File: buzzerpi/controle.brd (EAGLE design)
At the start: 100 x 80 mm, 10 parts, among them IC1 ULN2003AN, IC2 ULN2003AN

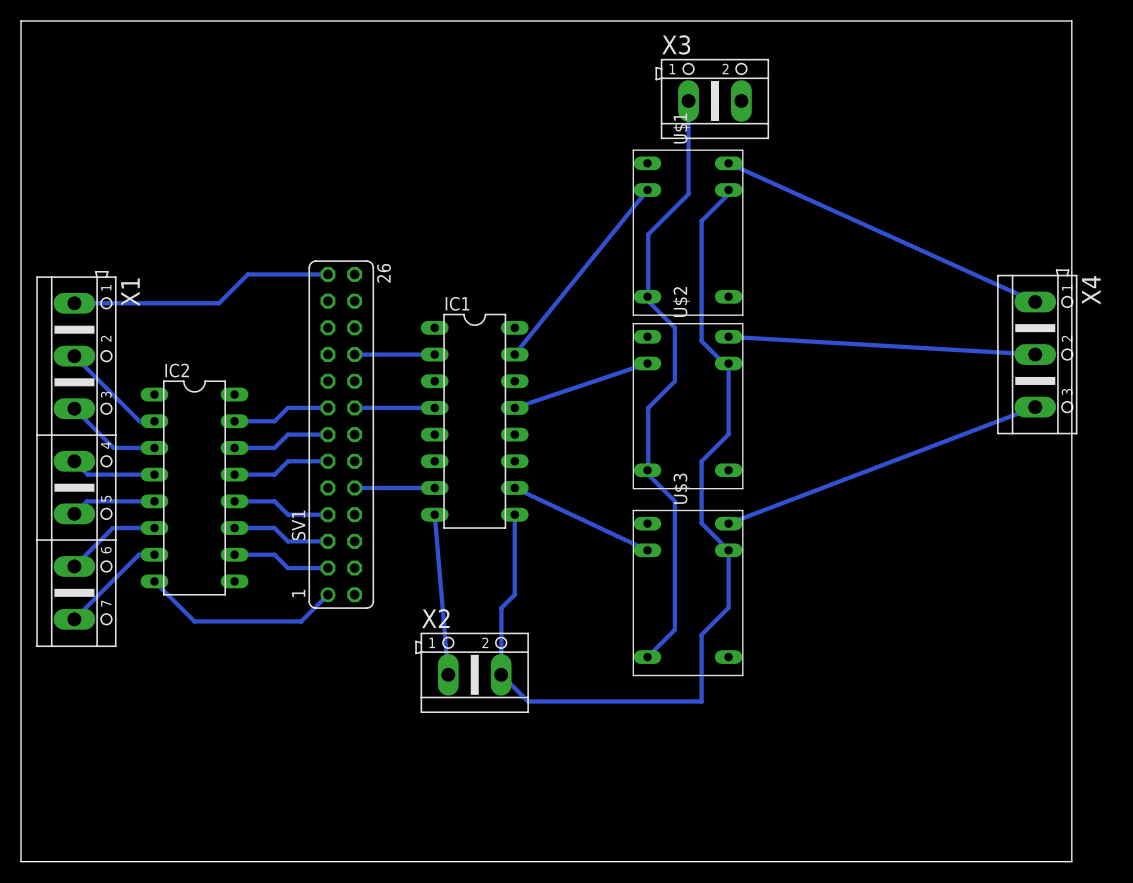
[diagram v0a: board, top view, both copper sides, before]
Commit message: layout geändert
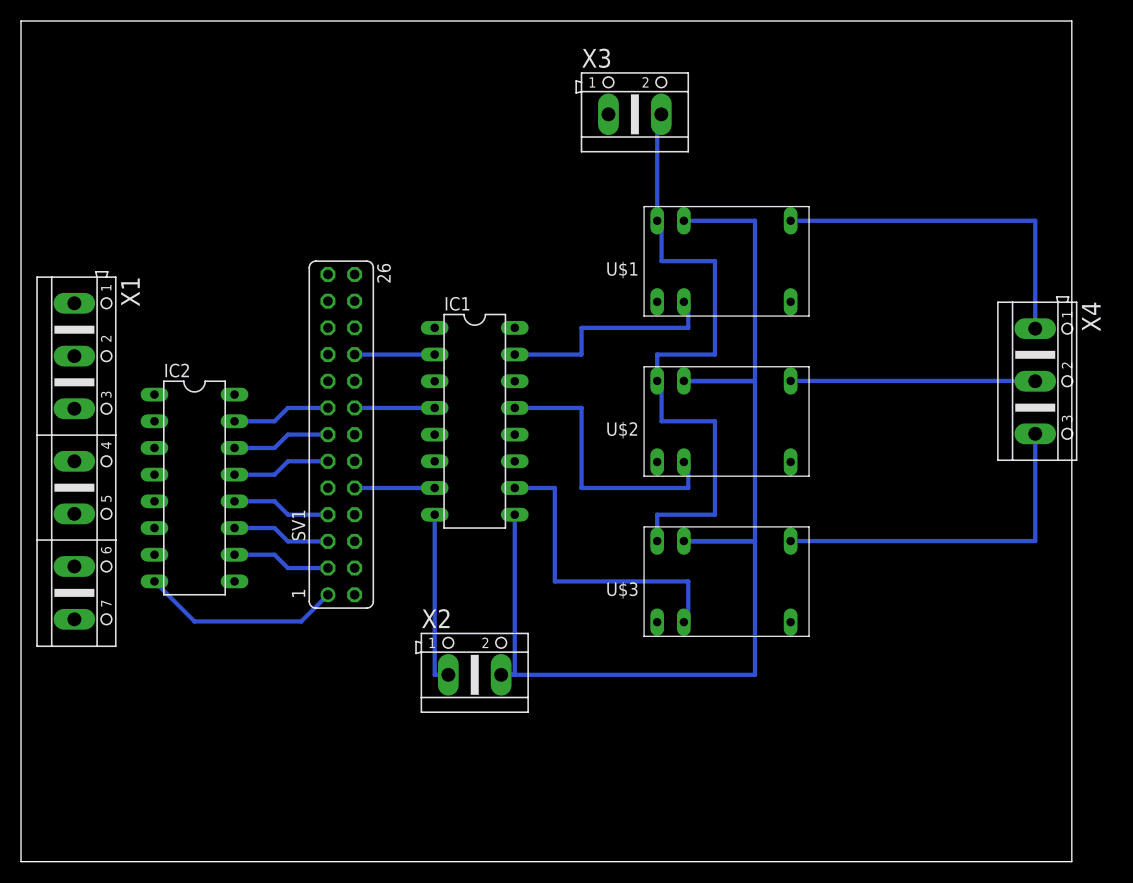
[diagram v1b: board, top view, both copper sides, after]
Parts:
- moved X3 7.73 mm to (58.4, 71.1)
- moved U$1 4.58 mm to (67.3, 57.1), turned to 180 degrees
- moved U$2 4.02 mm to (67.3, 41.9), turned to 180 degrees
- moved U$3 4.02 mm to (67.3, 26.7), turned to 180 degrees
- moved X4 2.54 mm to (96.5, 45.7)
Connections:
- removed net N$27: U$1.CENTER1, U$2.CENTER1, U$3.CENTER1, X3.1
- removed net N$28: U$2.CON1OPTION, X4.2
- removed net N$29: U$1.CON1OPTION, X4.1
- removed net N$30: U$3.CON1OPTION, X4.3
- new net N$22: U$1.CON1OPTION, U$2.CON1OPTION, U$3.CON1OPTION, X3.2
- new net N$23: U$1.CENTER2, X4.1
- new net N$25: U$2.CENTER2, X4.2
- new net N$26: U$3.CENTER2, X4.3
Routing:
- net N$22: track 0.00 -> 63.0 mm
- net N$27: track 58.9 -> 0.00 mm
- net N$23: track 0.00 -> 33.5 mm
- net N$26: track 0.00 -> 33.5 mm
- net N$29: track 32.0 -> 0.00 mm
- net N$30: track 31.2 -> 0.00 mm
- net N$28: track 29.2 -> 0.00 mm
- net N$24: track 90.7 -> 117.9 mm
- net N$8: track 25.3 -> 0.00 mm
- net N$25: track 0.00 -> 23.3 mm
- net N$20: track 14.0 -> 29.7 mm
- net N$16: track 13.3 -> 27.0 mm
- net N$9: track 10.2 -> 0.00 mm
- net N$14: track 10.2 -> 0.00 mm
- net N$10: track 9.17 -> 0.00 mm
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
